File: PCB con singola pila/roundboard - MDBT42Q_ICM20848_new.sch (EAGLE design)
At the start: 24 parts, among them U1 ICM-20948, U3 ADP1606ACPZN1.8-R7CP_6_3_ADI-L, X2 32.768kHz

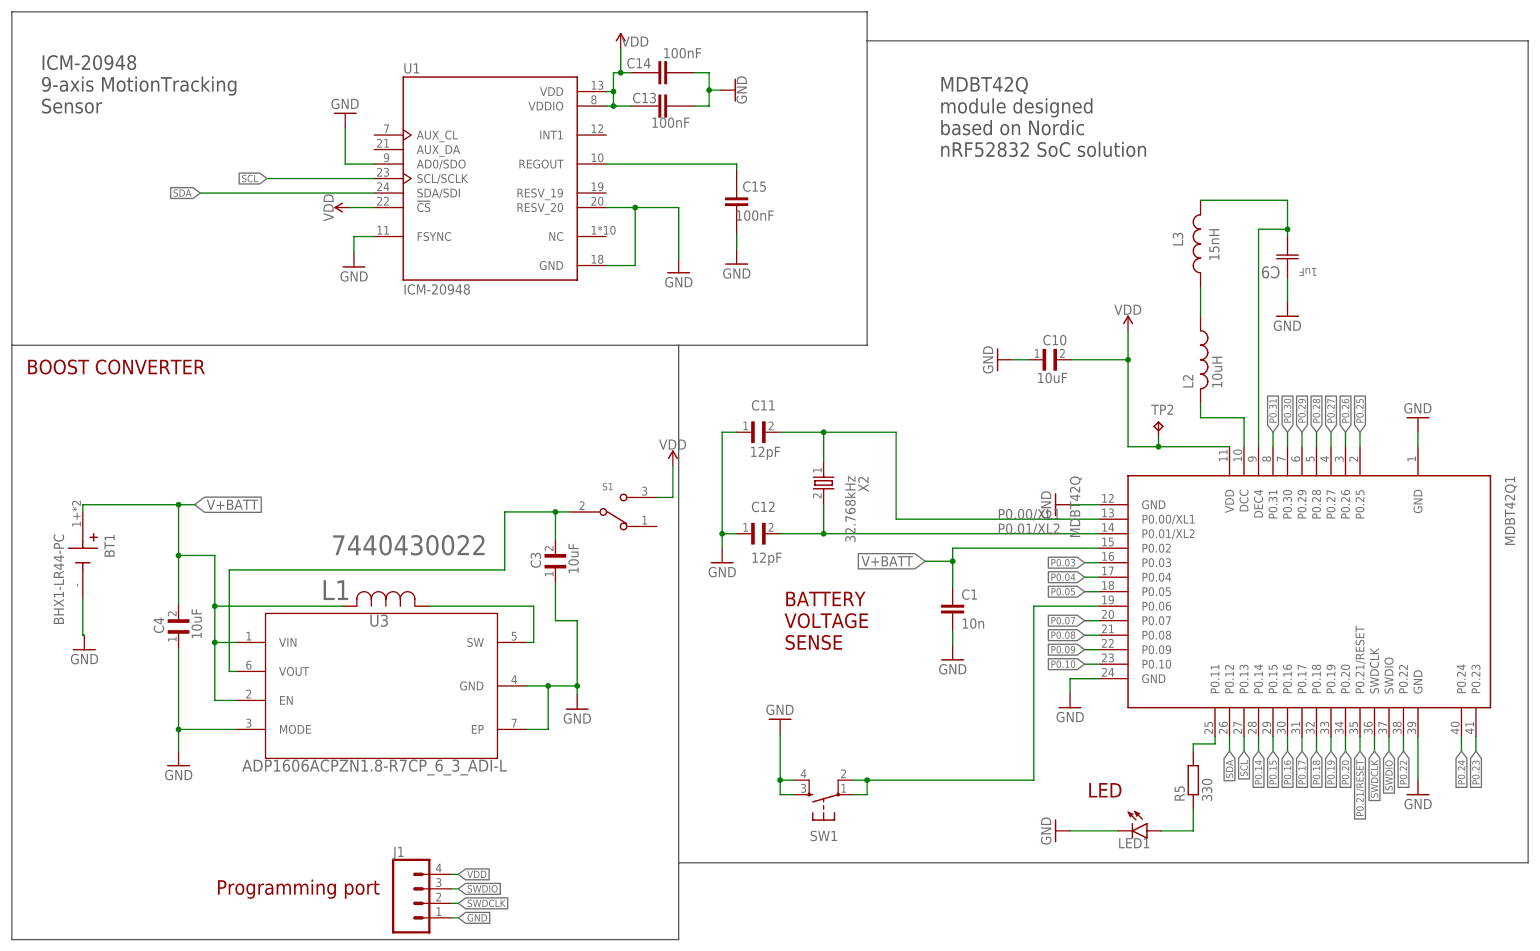
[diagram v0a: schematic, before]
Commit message: Led più grande (1206)
Tolti anche vari componenti inutili come le resistenze di pull up per i2c (già integrate nell'nrf) e la resistenza su INT dell'ICM
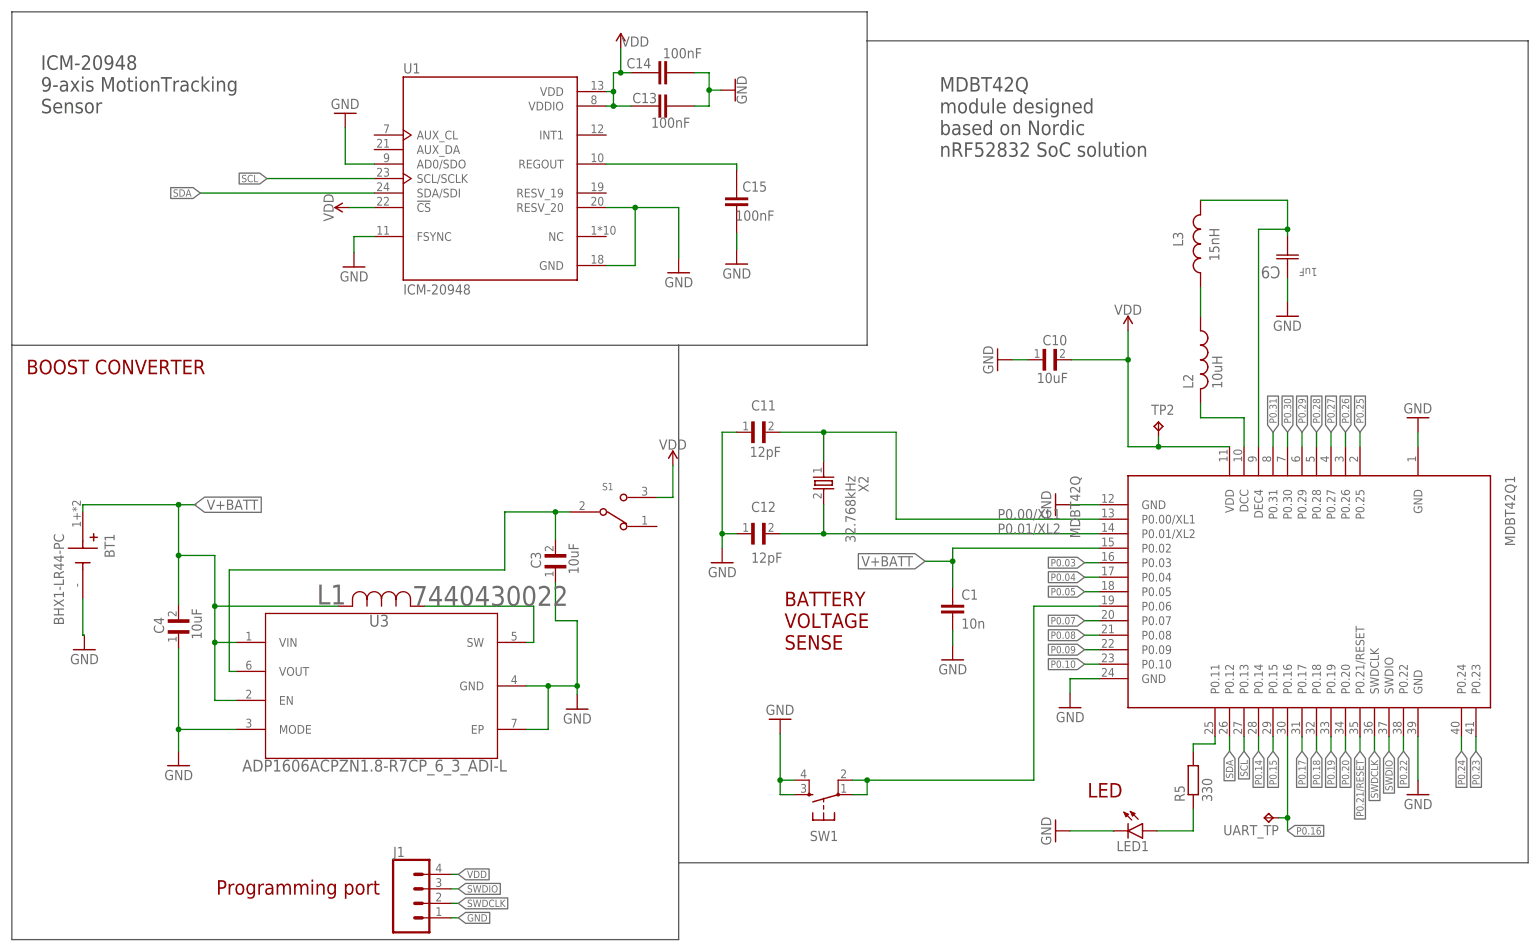
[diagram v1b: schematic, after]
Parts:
- added UART_TP: TPB1,27, testpad:TPB1,27
- LED1: device led:LEDCHIPLED_0603 -> led:LEDCHIPLED_1206
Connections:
- net P0.16: now also UART_TP.TP
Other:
- moved on the sheet: LED1
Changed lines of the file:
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@@
 <part name="U1" library="ICM-20948" deviceset="ICM-20948" device="" override_package3d_urn="urn:adsk.eagle:package:27670819/2" override_package_urn="urn:adsk.eagle:footprint:27670821/1"/>
 <part name="TP2" library="testpad" library_urn="urn:adsk.eagle:library:385" deviceset="TP" device="B1,27" package3d_urn="urn:adsk.eagle:package:27944/2"/>
-<part name="L1" library="inductor" deviceset="7440430022" device="" override_package3d_urn="urn:adsk.eagle:package:27725381/2" override_package_urn="urn:adsk.eagle:footprint:27725382/1" override_locally_modified="yes"/>
 <part name="R5" library="rcl" library_urn="urn:adsk.eagle:library:334" deviceset="R-EU_" device="R0603" package3d_urn="urn:adsk.eagle:package:23555/3" value="330"/>
-<part name="LED1" library="led" library_urn="urn:adsk.eagle:library:259" deviceset="LED" device="CHIPLED_0603" package3d_urn="urn:adsk.eagle:package:15822/2"/>
 <part name="C1" library="rcl" library_urn="urn:adsk.eagle:library:334" deviceset="C-EU" device="C0603" package3d_urn="urn:adsk.eagle:package:23616/2" value="10n"/>
 <part name="GND5" library="supply1" deviceset="GND" device=""/>
+<part name="UART_TP" library="testpad" library_urn="urn:adsk.eagle:library:385" deviceset="TP" device="B1,27" package3d_urn="urn:adsk.eagle:package:27944/2"/>
+<part name="L1" library="inductor" deviceset="7440430022" device=""/>
+<part name="LED1" library="led" library_urn="urn:adsk.eagle:library:259" deviceset="LED" device="CHIPLED_1206" package3d_urn="urn:adsk.eagle:package:15823/2"/>
 </parts>
 <sheets>
@@
 <attribute name="TP_SIGNAL_NAME" x="19.304" y="114.808" size="1.778" layer="97"/>
 </instance>
-<instance part="L1" gate="A" x="-124.968" y="83.82" smashed="yes">
-<attribute name="VALUE" x="-126.9492" y="92.7608" size="3.4798" layer="96" ratio="10" rot="SR0"/>
-<attribute name="NAME" x="-128.6764" y="84.8868" size="3.4798" layer="95" ratio="10" rot="SR0"/>
-</instance>
 <instance part="R5" gate="G$1" x="24.13" y="53.34" smashed="yes" rot="R90">
 <attribute name="NAME" x="22.6314" y="49.53" size="1.778" layer="95" rot="R90"/>
 <attribute name="VALUE" x="27.432" y="49.53" size="1.778" layer="96" rot="R90"/>
 </instance>
-<instance part="LED1" gate="G$1" x="16.002" y="44.45" smashed="yes" rot="R270">
-<attribute name="NAME" x="10.922" y="41.402" size="1.778" layer="95"/>
-<attribute name="VALUE" x="11.43" y="38.735" size="1.778" layer="96"/>
-</instance>
 <instance part="C1" gate="G$1" x="-18.034" y="84.582" smashed="yes">
 <attribute name="NAME" x="-16.51" y="84.963" size="1.778" layer="95"/>
@@
 <instance part="GND5" gate="1" x="-18.034" y="74.422" smashed="yes" rot="MR0">
 <attribute name="VALUE" x="-15.494" y="71.882" size="1.778" layer="96" rot="MR0"/>
+</instance>
+<instance part="UART_TP" gate="G$1" x="36.576" y="46.736" smashed="yes" rot="R90">
+<attribute name="NAME" x="39.116" y="45.466" size="1.778" layer="95" rot="R180"/>
+<attribute name="TP_SIGNAL_NAME" x="37.846" y="48.006" size="1.778" layer="97" rot="R90"/>
+</instance>
+<instance part="L1" gate="G$1" x="-125.73" y="83.82" smashed="yes">
+<attribute name="VALUE" x="-112.7252" y="83.8708" size="3.4798" layer="96" ratio="10" rot="SR0"/>
+<attribute name="NAME" x="-129.4384" y="84.1248" size="3.4798" layer="95" ratio="10" rot="SR0"/>
+</instance>
+<instance part="LED1" gate="G$1" x="15.24" y="44.45" smashed="yes" rot="R270">
+<attribute name="NAME" x="10.668" y="40.894" size="1.778" layer="95"/>
+<attribute name="VALUE" x="10.668" y="38.735" size="1.778" layer="96"/>
 </instance>
 </instances>
@@
 </segment>
 <segment>
-<wire x1="2.54" y1="44.45" x2="10.922" y2="44.45" width="0.1524" layer="91"/>
+<wire x1="2.54" y1="44.45" x2="10.16" y2="44.45" width="0.1524" layer="91"/>
 <pinref part="GND13" gate="1" pin="GND"/>
 <pinref part="LED1" gate="G$1" pin="C"/>
@@
 <net name="P0.16" class="0">
 <segment>
-<wire x1="40.64" y1="60.96" x2="40.64" y2="58.42" width="0.1524" layer="91"/>
-<label x="40.64" y="58.42" size="1.27" layer="95" rot="R270" xref="yes"/>
+<wire x1="40.64" y1="60.96" x2="40.64" y2="46.736" width="0.1524" layer="91"/>
+<label x="40.64" y="44.45" size="1.27" layer="95" xref="yes"/>
 <pinref part="MDBT42Q1" gate="G$1" pin="P0.16"/>
+<pinref part="UART_TP" gate="G$1" pin="TP"/>
+<wire x1="40.64" y1="46.736" x2="40.64" y2="44.45" width="0.1524" layer="91"/>
+<wire x1="39.116" y1="46.736" x2="40.64" y2="46.736" width="0.1524" layer="91"/>
+<junction x="40.64" y="46.736"/>
 </segment>
 </net>
@@
 <wire x1="-147.32" y1="92.71" x2="-153.67" y2="92.71" width="0.1524" layer="91"/>
 <junction x="-153.67" y="92.71"/>
-<wire x1="-124.968" y1="83.82" x2="-147.32" y2="83.82" width="0.1524" layer="91"/>
+<wire x1="-125.73" y1="83.82" x2="-147.32" y2="83.82" width="0.1524" layer="91"/>
 <junction x="-147.32" y="83.82"/>
 <wire x1="-147.32" y1="67.31" x2="-147.32" y2="77.47" width="0.1524" layer="91"/>
@@
 <wire x1="-170.45" y1="100.33" x2="-170.45" y2="101.6" width="0.1524" layer="91"/>
 <wire x1="-170.45" y1="101.6" x2="-153.67" y2="101.6" width="0.1524" layer="91"/>
-<pinref part="L1" gate="A" pin="2"/>
 <label x="-150.876" y="101.6" size="1.778" layer="95" xref="yes"/>
 <wire x1="-153.67" y1="101.6" x2="-150.622" y2="101.6" width="0.1524" layer="91"/>
 <junction x="-153.67" y="101.6"/>
+<pinref part="L1" gate="G$1" pin="2"/>
 </segment>
 </net>
@@
 <net name="N$1" class="0">
 <segment>
-<wire x1="18.542" y1="44.45" x2="24.13" y2="44.45" width="0.1524" layer="91"/>
+<wire x1="17.78" y1="44.45" x2="24.13" y2="44.45" width="0.1524" layer="91"/>
 <wire x1="24.13" y1="44.45" x2="24.13" y2="48.26" width="0.1524" layer="91"/>
 <pinref part="R5" gate="G$1" pin="1"/>
@@
 <segment>
 <wire x1="-91.44" y1="77.47" x2="-91.44" y2="83.82" width="0.1524" layer="91"/>
-<wire x1="-91.44" y1="83.82" x2="-109.728" y2="83.82" width="0.1524" layer="91"/>
+<wire x1="-91.44" y1="83.82" x2="-110.49" y2="83.82" width="0.1524" layer="91"/>
 <pinref part="U3" gate="A" pin="SW"/>
 <wire x1="-91.44" y1="77.47" x2="-92.71" y2="77.47" width="0.1524" layer="91"/>
-<pinref part="L1" gate="A" pin="1"/>
-</segment>
-</net>
+<pinref part="L1" gate="G$1" pin="1"/>
+</segment>
+</net>
